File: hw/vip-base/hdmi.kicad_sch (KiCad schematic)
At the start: 1 part

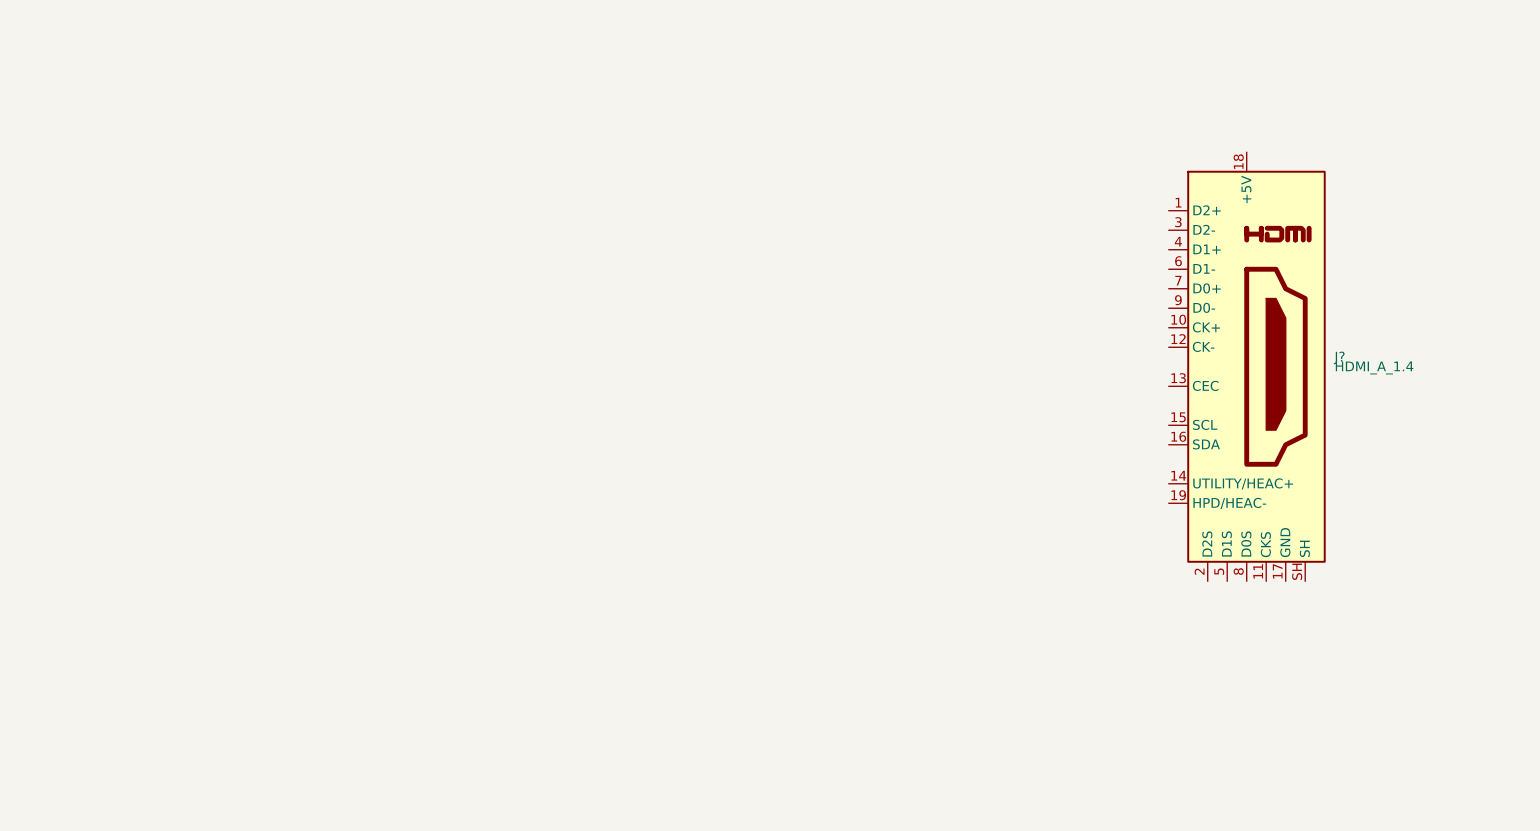
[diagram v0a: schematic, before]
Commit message: hw: Finish main routing
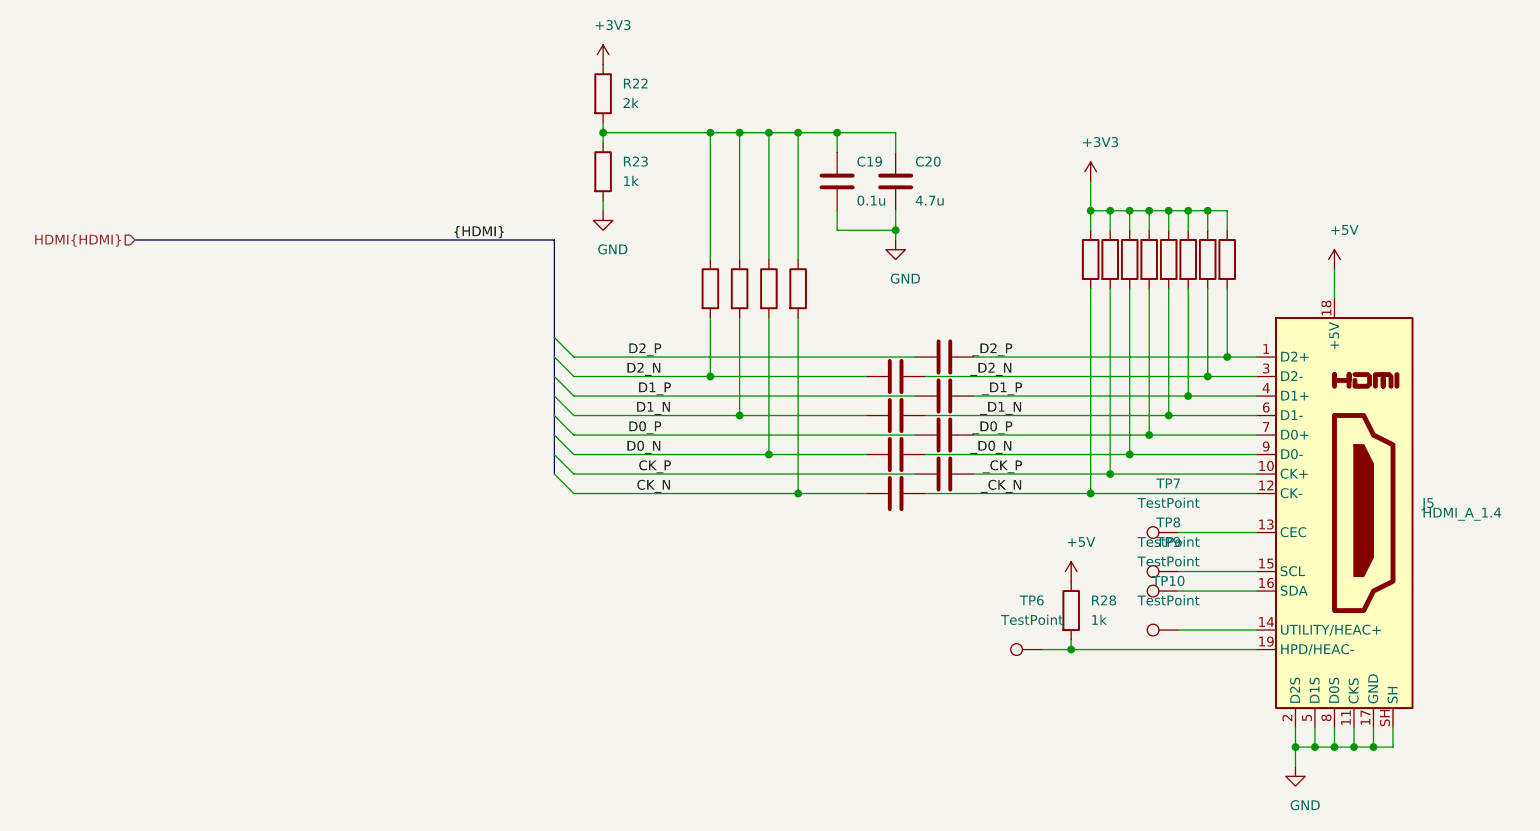
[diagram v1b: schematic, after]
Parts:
- added C19, C21, C22, C23, C24, C25, C26, C27, C28: 0.1u, Capacitor_SMD:C_0402_1005Metric, symbol Device:C
- added C20: 4.7u, Capacitor_SMD:C_0402_1005Metric, symbol Device:C
- added R22: 2k, Resistor_SMD:R_0402_1005Metric, symbol Device:R
- added R23, R28: 1k, Resistor_SMD:R_0402_1005Metric, symbol Device:R
- added R24, R25, R26, R27: 47k, Resistor_SMD:R_0402_1005Metric, symbol Device:R
- added R29, R30, R31, R32, R33, R34, R35, R36: 50R, Resistor_SMD:R_0402_1005Metric, symbol Device:R
- added TP10, TP6, TP7, TP8, TP9: TestPoint, TestPoint:TestPoint_THTPad_D1.5mm_Drill0.7mm, symbol Connector:TestPoint
- J5: renamed from J?; footprint (none) -> vip-base:HDMI-10029449-111RLF
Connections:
- net _D2_P: now reaches J5.1 (D2+)
- net _D2_P: now also C25.2, R36.2
- net _CK_P: now reaches J5.10 (CK+)
- net _CK_P: now also C28.2, R30.2
- net GND: now reaches J5.11 (CKS)
- net GND: now also J5.17 (GND), J5.2 (D2S), J5.5 (D1S), J5.8 (D0S), J5.SH, C19.2, C20.2, R23.2
- net _CK_N: now reaches J5.12 (CK-)
- net _CK_N: now also C24.2, R29.2
- net at J5.13 (CEC): now also TP7.1
- net at J5.14 (UTILITY/HEAC+): now also TP10.1
- net at J5.15 (SCL): now also TP8.1
- net at J5.16 (SDA): now also TP9.1
- net +5V: now reaches J5.18 (+5V)
- net +5V: now also R28.1
- net at J5.19 (HPD/HEAC-): now also R28.2, TP6.1
- net _D2_N: now reaches J5.3 (D2-)
- net _D2_N: now also C21.2, R35.2
- net _D1_P: now reaches J5.4 (D1+)
- net _D1_P: now also C26.2, R34.2
- net _D1_N: now reaches J5.6 (D1-)
- net _D1_N: now also C22.2, R33.2
- net _D0_P: now reaches J5.7 (D0+)
- net _D0_P: now also C27.2, R32.2
- net _D0_N: now reaches J5.9 (D0-)
- net _D0_N: now also C23.2, R31.2
- new net: C19.1, C20.1, R22.2, R23.1, R24.1, R25.1, R26.1, R27.1
- new net +3V3: R22.1, R29.1, R30.1, R31.1, R32.1, R33.1, R34.1, R35.1, R36.1
- new net CK_N: C24.1, R27.2
- new net CK_P: C28.1
- new net D0_N: C23.1, R26.2
- new net D0_P: C27.1
- new net D1_N: C22.1, R25.2
- new net D1_P: C26.1
- new net D2_N: C21.1, R24.2
- new net D2_P: C25.1
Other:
- company: (none) -> GsD
- title: (none) -> VIP Base
- moved on the sheet: J5
